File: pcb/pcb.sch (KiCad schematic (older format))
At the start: 16 parts, among them J1 BAT+, J2 BAT-, SW1 Reset, SW2 Flash, U1 BOB-13263, U2 ESP-12F, U3 TP4056, U4 GY-521, U5 MCP1700

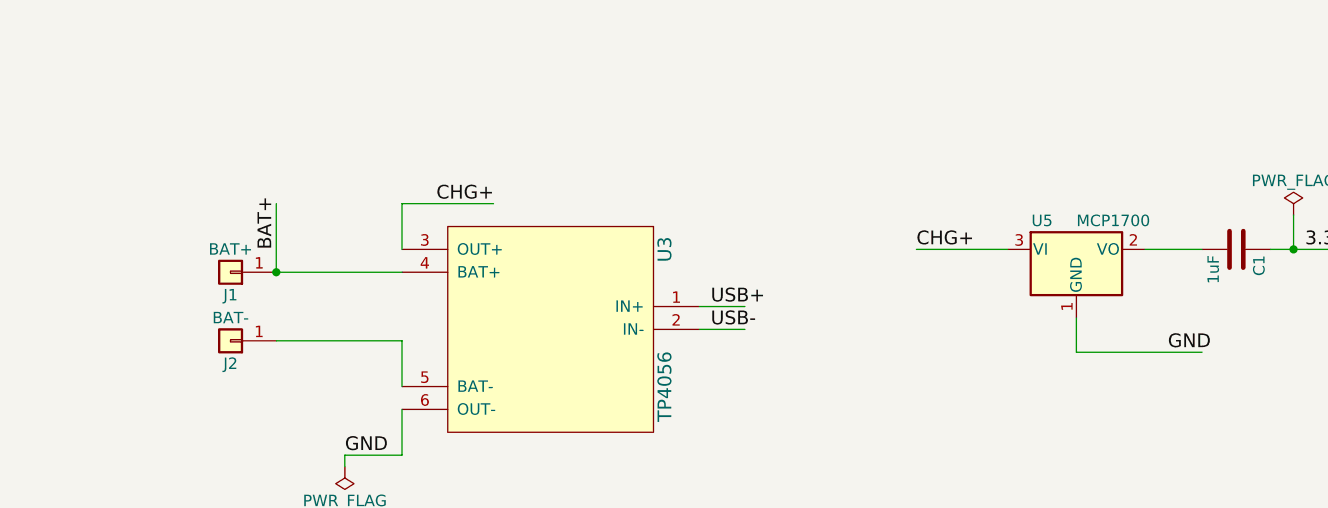
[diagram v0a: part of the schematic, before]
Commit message: Move KiCad libraries into project
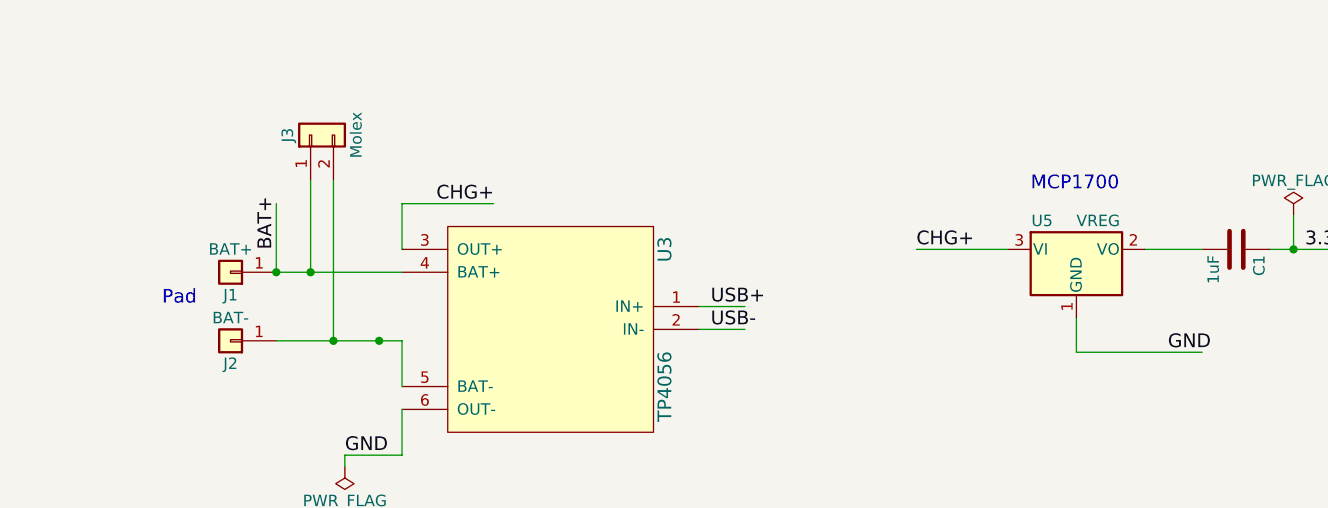
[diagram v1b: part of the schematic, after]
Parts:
- added J3: Molex, Connectors_Molex:Molex_PicoBlade_53047-0210_02x1.25mm_Straight, symbol Conn_01x02
- J1, J2: footprint Wire_Pads:SolderWirePad_single_SMD_5x10mm -> Extra_Pads:SolderWirePad_single_SMD_5x3mm
- U5: value MCP1700 -> VREG
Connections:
- wire segments 58 -> 60
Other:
- note added: "MCP1700"
- note added: "Pad"
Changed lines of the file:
@@
 P 9450 2250
 F 0 "U5" H 9300 2375 50  0000 C CNN
-F 1 "MCP1700" H 9450 2375 50  0000 L CNN
+F 1 "VREG" H 9450 2375 50  0000 L CNN
 F 2 "TO_SOT_Packages_SMD:SOT-23" H 9450 2475 50  0001 C CNN
 F 3 "" H 9450 2250 50  0001 C CNN
@@
 F 0 "J1" H 5750 2450 50  0000 C CNN
 F 1 "BAT+" H 5750 2250 50  0000 C CNN
-F 2 "Wire_Pads:SolderWirePad_single_SMD_5x10mm" H 5750 2350 50  0001 C CNN
+F 2 "Extra_Pads:SolderWirePad_single_SMD_5x3mm" H 5750 2350 50  0001 C CNN
 F 3 "" H 5750 2350 50  0001 C CNN
 	1    5750 2350
@@
 F 0 "J2" H 5750 2750 50  0000 C CNN
 F 1 "BAT-" H 5750 2550 50  0000 C CNN
-F 2 "Wire_Pads:SolderWirePad_single_SMD_5x10mm" H 5750 2650 50  0001 C CNN
+F 2 "Extra_Pads:SolderWirePad_single_SMD_5x3mm" H 5750 2650 50  0001 C CNN
 F 3 "" H 5750 2650 50  0001 C CNN
 	1    5750 2650
@@
 NoConn ~ 2400 2450
 NoConn ~ 2400 2350
-Wire Wire Line
-	3000 1650 4200 1650
-Wire Wire Line
-	3000 1650 3000 1800
-Connection ~ 3000 1650
-Connection ~ 3800 1650
-Wire Wire Line
-	8000 2500 7800 2500
-Wire Wire Line
-	8000 2600 7800 2600
-Wire Wire Line
-	6500 2950 6500 3150
-Wire Wire Line
-	6500 3150 6250 3150
-Wire Wire Line
-	6500 2250 6500 2050
-Wire Wire Line
-	6500 2050 6900 2050
-Wire Wire Line
-	8750 2250 9150 2250
-Wire Wire Line
-	9450 2550 9450 2700
-Wire Wire Line
-	9450 2700 10000 2700
-Wire Wire Line
-	9750 2250 10000 2250
-Wire Wire Line
-	5950 2350 6500 2350
-Wire Wire Line
-	2000 5700 2400 5700
-Wire Wire Line
-	4500 5600 4900 5600
-Wire Wire Line
-	4500 5700 4900 5700
-Wire Wire Line
-	4500 5800 4900 5800
-Wire Wire Line
-	4500 5900 4900 5900
-Wire Wire Line
-	1700 6300 2700 6300
-Wire Wire Line
-	4500 6300 5600 6300
-Wire Wire Line
-	7500 5300 7800 5300
-Wire Wire Line
-	7500 5400 7800 5400
-Wire Wire Line
-	7500 5500 7800 5500
-Wire Wire Line
-	7500 5600 7800 5600
-Wire Wire Line
-	7500 5900 7800 5900
-Wire Wire Line
-	5600 6100 4800 6100
-Wire Wire Line
-	2650 5250 2650 5600
-Wire Wire Line
-	2300 5400 2650 5400
-Wire Wire Line
-	1700 5400 2000 5400
-Wire Wire Line
-	2650 4850 2650 4700
-Connection ~ 2650 5400
-Wire Wire Line
-	1700 5800 2400 5800
-Wire Wire Line
-	1700 5400 1700 6300
-Connection ~ 1700 5400
-Wire Wire Line
-	2000 6000 2700 6000
-Wire Wire Line
-	4500 6000 5300 6000
-Wire Wire Line
-	5150 5200 5150 6000
-Connection ~ 5150 6000
-Wire Wire Line
-	5150 4700 5150 4800
-Wire Wire Line
-	2650 4700 5150 4700
-Wire Wire Line
-	3900 4700 3900 4450
-Connection ~ 3900 4700
-Connection ~ 1700 5800
-Wire Wire Line
-	5600 5700 5600 6100
-Connection ~ 5600 6000
-Wire Wire Line
-	4500 6200 4750 6200
-Wire Wire Line
-	5050 6200 5200 6200
-Wire Wire Line
-	5200 6200 5200 6300
-Connection ~ 5200 6300
-Wire Wire Line
-	2650 5600 2700 5600
-Wire Wire Line
-	10300 2250 10650 2250
-Wire Wire Line
-	10400 2100 10400 2250
-Connection ~ 10400 2250
-Wire Wire Line
-	2350 6050 2350 6000
-Connection ~ 2350 6000
-Wire Wire Line
-	5950 2350 5950 2050
-Connection ~ 5950 2350
-Wire Wire Line
-	3200 1800 3200 1750
-Wire Wire Line
-	3200 1750 4200 1750
-Wire Wire Line
-	3800 1600 3800 1650
-Wire Wire Line
-	3800 1800 3800 1750
-Connection ~ 3800 1750
-Wire Wire Line
-	2800 1800 2800 1350
-Wire Wire Line
-	2800 1350 3250 1350
-Wire Wire Line
-	2900 1450 2900 1800
-Wire Wire Line
-	2900 1450 3250 1450
-Wire Wire Line
-	5950 2650 6500 2650
-Wire Wire Line
-	6500 2650 6500 2850
 $Comp
 L PWR_FLAG #FLG05
@@
 $EndComp
 Wire Wire Line
+	3000 1650 4200 1650
+Wire Wire Line
+	3000 1650 3000 1800
+Connection ~ 3000 1650
+Connection ~ 3800 1650
+Wire Wire Line
+	8000 2500 7800 2500
+Wire Wire Line
+	8000 2600 7800 2600
+Wire Wire Line
+	6500 2950 6500 3150
+Wire Wire Line
+	6500 3150 6250 3150
+Wire Wire Line
+	6500 2250 6500 2050
+Wire Wire Line
+	6500 2050 6900 2050
+Wire Wire Line
+	8750 2250 9150 2250
+Wire Wire Line
+	9450 2550 9450 2700
+Wire Wire Line
+	9450 2700 10000 2700
+Wire Wire Line
+	9750 2250 10000 2250
+Wire Wire Line
+	5950 2350 6500 2350
+Wire Wire Line
+	2000 5700 2400 5700
+Wire Wire Line
+	4500 5600 4900 5600
+Wire Wire Line
+	4500 5700 4900 5700
+Wire Wire Line
+	4500 5800 4900 5800
+Wire Wire Line
+	4500 5900 4900 5900
+Wire Wire Line
+	1700 6300 2700 6300
+Wire Wire Line
+	4500 6300 5600 6300
+Wire Wire Line
+	7500 5300 7800 5300
+Wire Wire Line
+	7500 5400 7800 5400
+Wire Wire Line
+	7500 5500 7800 5500
+Wire Wire Line
+	7500 5600 7800 5600
+Wire Wire Line
+	7500 5900 7800 5900
+Wire Wire Line
+	5600 6100 4800 6100
+Wire Wire Line
+	2650 5250 2650 5600
+Wire Wire Line
+	2300 5400 2650 5400
+Wire Wire Line
+	1700 5400 2000 5400
+Wire Wire Line
+	2650 4850 2650 4700
+Connection ~ 2650 5400
+Wire Wire Line
+	1700 5800 2400 5800
+Wire Wire Line
+	1700 5400 1700 6300
+Connection ~ 1700 5400
+Wire Wire Line
+	2000 6000 2700 6000
+Wire Wire Line
+	4500 6000 5300 6000
+Wire Wire Line
+	5150 5200 5150 6000
+Connection ~ 5150 6000
+Wire Wire Line
+	5150 4700 5150 4800
+Wire Wire Line
+	2650 4700 5150 4700
+Wire Wire Line
+	3900 4700 3900 4450
+Connection ~ 3900 4700
+Connection ~ 1700 5800
+Wire Wire Line
+	5600 5700 5600 6100
+Connection ~ 5600 6000
+Wire Wire Line
+	4500 6200 4750 6200
+Wire Wire Line
+	5050 6200 5200 6200
+Wire Wire Line
+	5200 6200 5200 6300
+Connection ~ 5200 6300
+Wire Wire Line
+	2650 5600 2700 5600
+Wire Wire Line
+	10300 2250 10650 2250
+Wire Wire Line
+	10400 2100 10400 2250
+Connection ~ 10400 2250
+Wire Wire Line
+	2350 6050 2350 6000
+Connection ~ 2350 6000
+Wire Wire Line
+	5950 2350 5950 2050
+Connection ~ 5950 2350
+Wire Wire Line
+	3200 1800 3200 1750
+Wire Wire Line
+	3200 1750 4200 1750
+Wire Wire Line
+	3800 1600 3800 1650
+Wire Wire Line
+	3800 1800 3800 1750
+Connection ~ 3800 1750
+Wire Wire Line
+	2800 1800 2800 1350
+Wire Wire Line
+	2800 1350 3250 1350
+Wire Wire Line
+	2900 1450 2900 1800
+Wire Wire Line
+	2900 1450 3250 1450
+Wire Wire Line
+	5950 2650 6500 2650
+Wire Wire Line
+	6500 2650 6500 2850
+Wire Wire Line
 	6250 3150 6250 3200
+Wire Wire Line
+	6100 1950 6100 2350
+Connection ~ 6100 2350
+Connection ~ 6400 2650
+Text Notes 5450 2500 0    60   ~ 0
+Pad
+$Comp
+L Conn_01x02 J3
+U 1 1 5B22789F
+P 6100 1750
+F 0 "J3" H 6100 1850 50  0000 C CNN
+F 1 "Molex" H 6100 1550 50  0000 C CNN
+F 2 "Connectors_Molex:Molex_PicoBlade_53047-0210_02x1.25mm_Straight" H 6100 1750 50  0001 C CNN
+F 3 "" H 6100 1750 50  0001 C CNN
+	1    6100 1750
+	0    -1   -1   0
+$EndComp
+Wire Wire Line
+	6200 1950 6200 2650
+Connection ~ 6200 2650
+Text Notes 9250 2000 0    60   ~ 0
+MCP1700
 $EndSCHEMATC

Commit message: Some ongoing minor PCB edits
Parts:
- added R2: 120k, Resistors_SMD:R_1206_HandSoldering, symbol R
- R3: renamed from R2; value 100k -> 390k
- renumbered R3 to R4, R4 to R5, R5 to R6, R6 to R7
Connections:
- wire segments 60 -> 63
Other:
- moved on the sheet: R3
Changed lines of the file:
@@
 Sheet 1 1
 Title "Pendulum PCB"
-Date "2018-06-13"
-Rev "0.0.1"
+Date "2018-06-14"
+Rev "0.0.2"
 Comp ""
 Comment1 ""
@@
 $EndDescr
 $Comp
-L R R2
+L R R3
 U 1 1 5B215E85
-P 2550 5700
-F 0 "R2" V 2630 5700 50  0000 C CNN
-F 1 "100k" V 2550 5700 50  0000 C CNN
-F 2 "Resistors_SMD:R_1206_HandSoldering" V 2480 5700 50  0001 C CNN
-F 3 "" H 2550 5700 50  0001 C CNN
-	1    2550 5700
+P 2400 5550
+F 0 "R3" V 2480 5550 50  0000 C CNN
+F 1 "390k" V 2400 5550 50  0000 C CNN
+F 2 "Resistors_SMD:R_1206_HandSoldering" V 2330 5550 50  0001 C CNN
+F 3 "" H 2400 5550 50  0001 C CNN
+	1    2400 5550
 	0    -1   -1   0
 $EndComp
@@
 $EndComp
 $Comp
-L R R4
+L R R5
 U 1 1 5B21A80E
 P 4650 6100
-F 0 "R4" V 4730 6100 50  0000 C CNN
+F 0 "R5" V 4730 6100 50  0000 C CNN
 F 1 "10k" V 4650 6100 50  0000 C CNN
 F 2 "Resistors_SMD:R_1206_HandSoldering" V 4580 6100 50  0001 C CNN
@@
 $EndComp
 $Comp
-L R R3
+L R R4
 U 1 1 5B21AA4B
 P 2550 5800
-F 0 "R3" V 2630 5800 50  0000 C CNN
+F 0 "R4" V 2630 5800 50  0000 C CNN
 F 1 "10k" V 2550 5800 50  0000 C CNN
 F 2 "Resistors_SMD:R_1206_HandSoldering" V 2480 5800 50  0001 C CNN
@@
 $EndComp
 $Comp
-L R R6
+L R R7
 U 1 1 5B21AAD4
 P 5450 6000
-F 0 "R6" V 5530 6000 50  0000 C CNN
+F 0 "R7" V 5530 6000 50  0000 C CNN
 F 1 "10k" V 5450 6000 50  0000 C CNN
 F 2 "Resistors_SMD:R_1206_HandSoldering" V 5380 6000 50  0001 C CNN
@@
 Text Label 3950 1750 0    60   ~ 0
 USB-
-Text Label 2000 5700 0    60   ~ 0
+Text Label 1800 5550 0    60   ~ 0
 BAT+
 Text Label 4750 5800 0    60   ~ 0
@@
 GY+
 $Comp
-L R R5
+L R R6
 U 1 1 5B228DC8
 P 4900 6200
-F 0 "R5" V 4980 6200 50  0000 C CNN
+F 0 "R6" V 4980 6200 50  0000 C CNN
 F 1 "10k" V 4900 6200 50  0000 C CNN
 F 2 "Resistors_SMD:R_1206_HandSoldering" V 4830 6200 50  0001 C CNN
@@
 Wire Wire Line
 	3000 1650 3000 1800
-Connection ~ 3000 1650
 Connection ~ 3800 1650
 Wire Wire Line
@@
 Wire Wire Line
 	5950 2350 6500 2350
-Wire Wire Line
-	2000 5700 2400 5700
 Wire Wire Line
 	4500 5600 4900 5600
@@
 Text Notes 9250 2000 0    60   ~ 0
 MCP1700
+$Comp
+L R R2
+U 1 1 5B228874
+P 2200 5700
+F 0 "R2" V 2280 5700 50  0000 C CNN
+F 1 "120k" V 2200 5700 50  0000 C CNN
+F 2 "Resistors_SMD:R_1206_HandSoldering" V 2130 5700 50  0001 C CNN
+F 3 "" H 2200 5700 50  0001 C CNN
+	1    2200 5700
+	0    -1   -1   0
+$EndComp
+Wire Wire Line
+	1800 5550 2250 5550
+Wire Wire Line
+	2550 5550 2550 5700
+Wire Wire Line
+	2350 5700 2700 5700
+Connection ~ 2550 5700
+Wire Wire Line
+	2050 5700 1800 5700
+Text Label 1800 5700 0    60   ~ 0
+GND
 $EndSCHEMATC

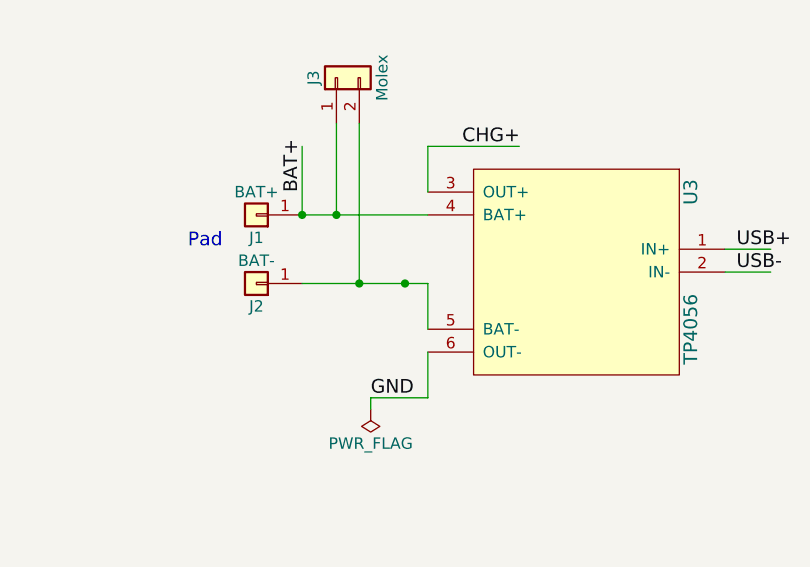
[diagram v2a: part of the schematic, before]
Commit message: Remove traces under ESP-12 antenna, switch to 90* Molex connector
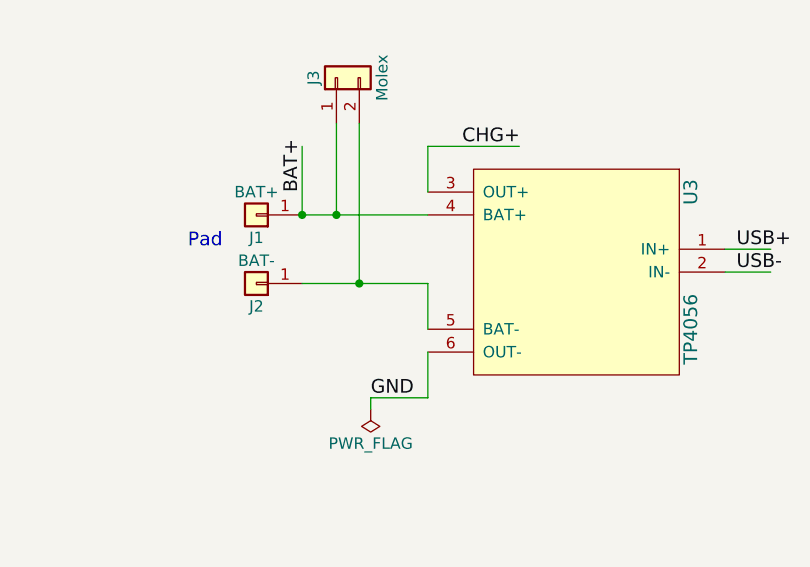
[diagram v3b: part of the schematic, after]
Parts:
- J3: footprint Connectors_Molex:Molex_PicoBlade_53047-0210_02x1.25mm_Straight -> Connectors_Molex:Molex_PicoBlade_53048-0210_02x1.25mm_Angled
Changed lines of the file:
@@
 	6100 1950 6100 2350
 Connection ~ 6100 2350
-Connection ~ 6400 2650
 Text Notes 5450 2500 0    60   ~ 0
 Pad
@@
 F 0 "J3" H 6100 1850 50  0000 C CNN
 F 1 "Molex" H 6100 1550 50  0000 C CNN
-F 2 "Connectors_Molex:Molex_PicoBlade_53047-0210_02x1.25mm_Straight" H 6100 1750 50  0001 C CNN
+F 2 "Connectors_Molex:Molex_PicoBlade_53048-0210_02x1.25mm_Angled" H 6100 1750 50  0001 C CNN
 F 3 "" H 6100 1750 50  0001 C CNN
 	1    6100 1750

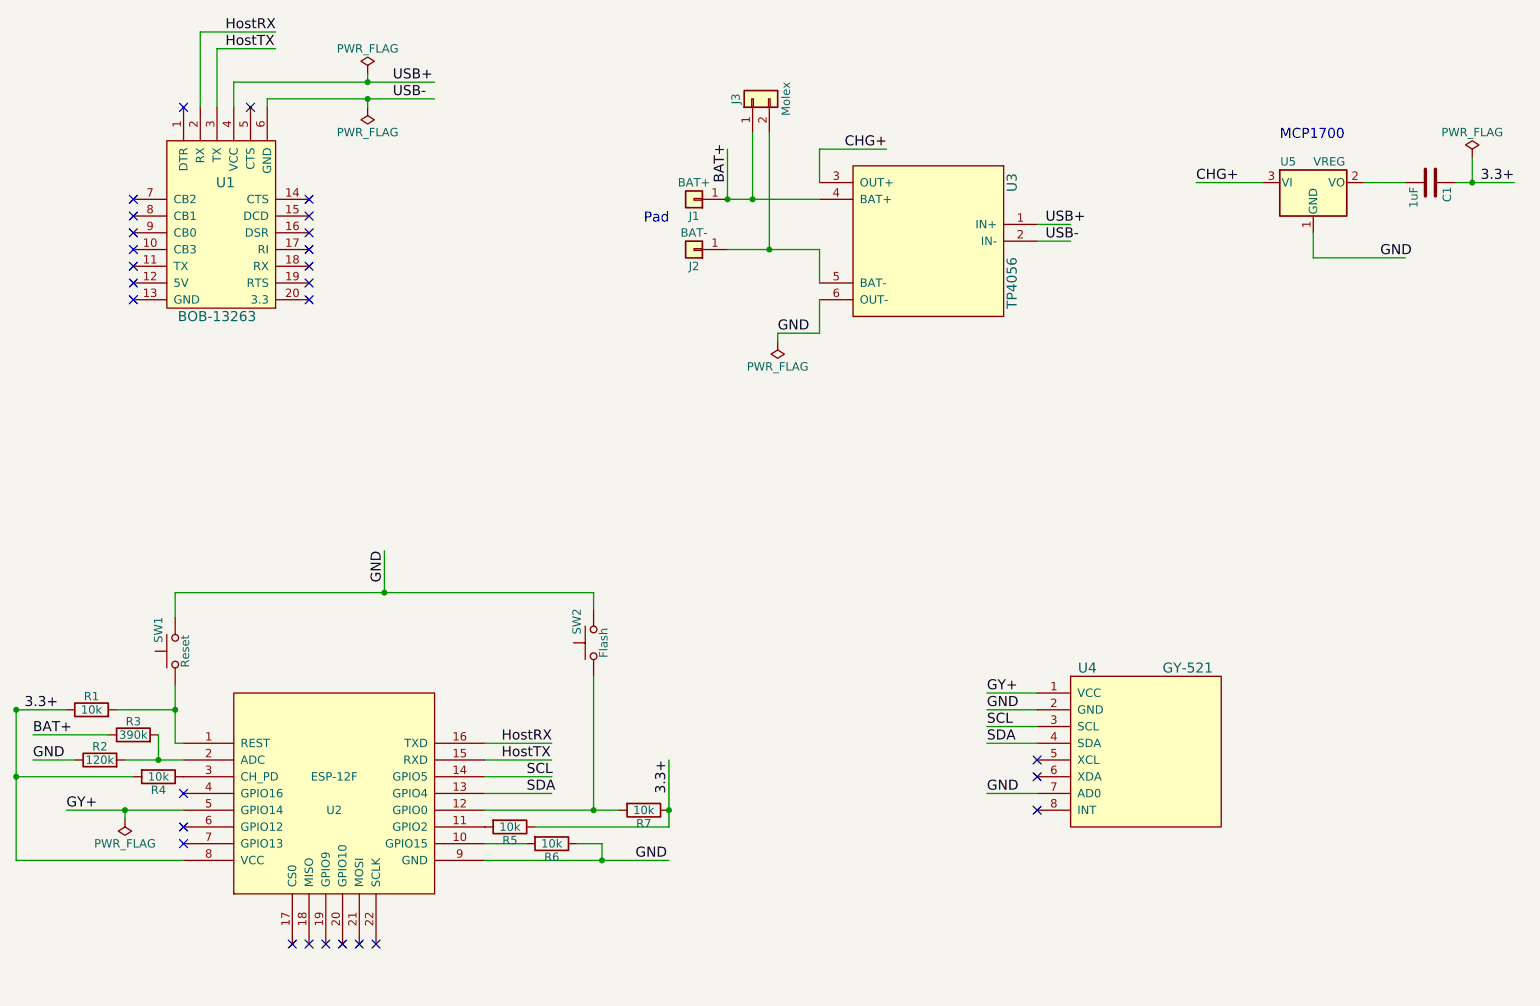
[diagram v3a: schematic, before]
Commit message: Switch to 8.5x11 paper
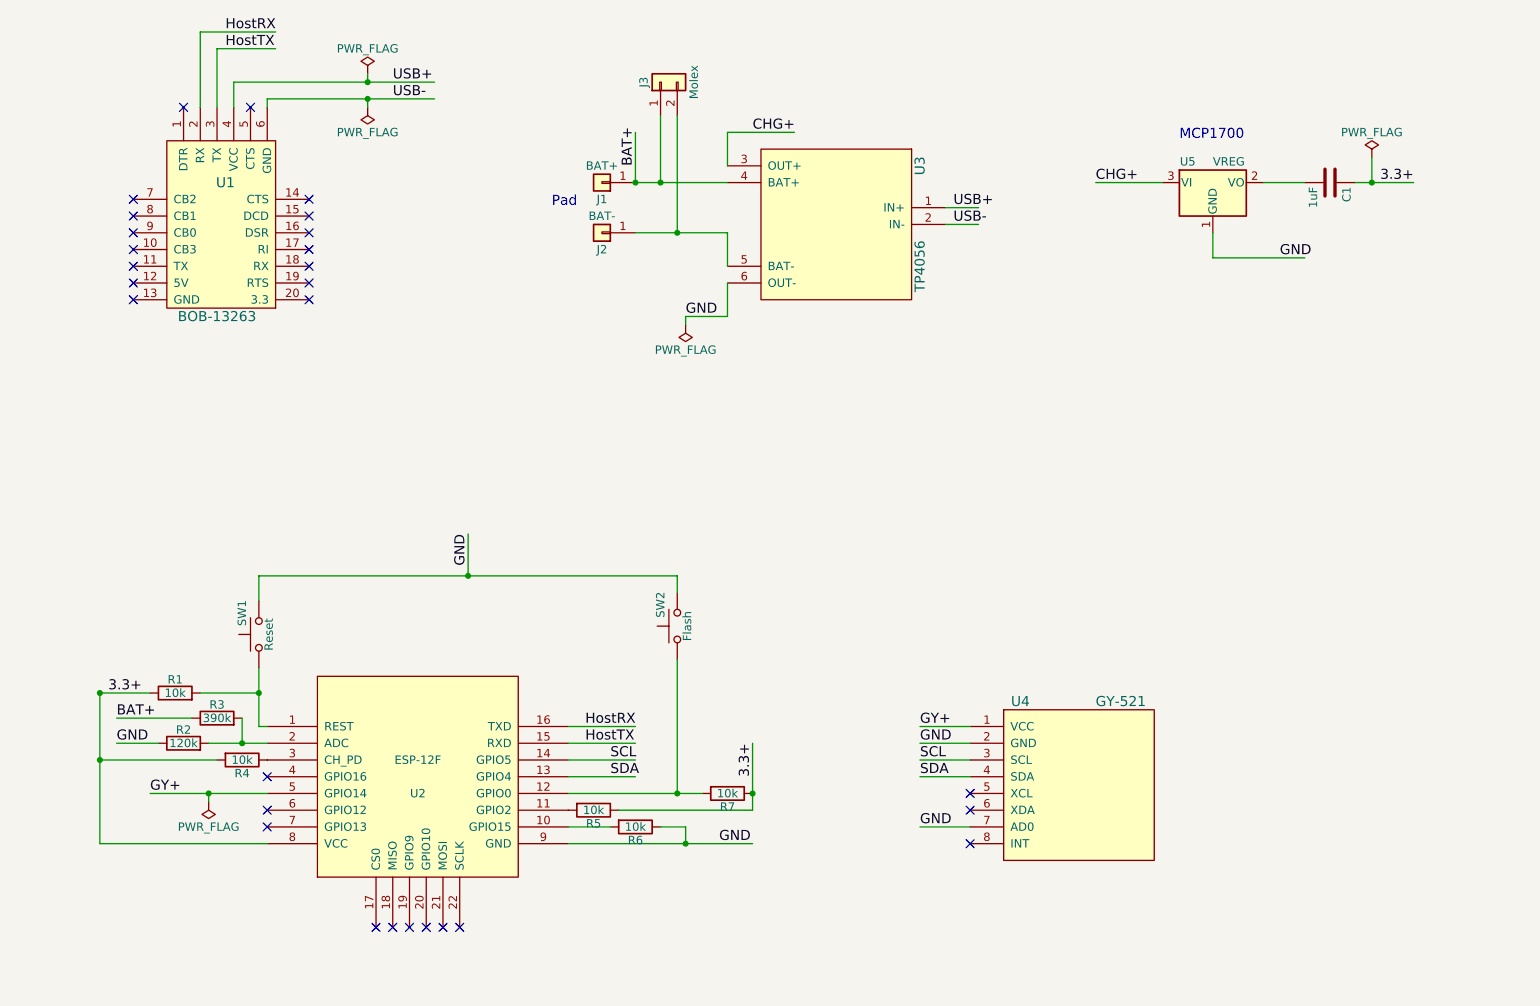
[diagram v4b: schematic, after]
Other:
- moved on the sheet: C1, J1, J2, J3, R1, R2, R3, R4, R5, R6, R7, SW1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
